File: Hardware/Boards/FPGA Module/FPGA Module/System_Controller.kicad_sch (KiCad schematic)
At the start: 0 parts

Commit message: FPGA Board schematic work
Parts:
- added C1, C10, C11, C5, C6, C7, C8, C9: 100nF, Capacitor_SMD:C_0201_0603Metric, symbol Device:C_Small
- added C12, C4: 1uF, Capacitor_SMD:C_0201_0603Metric, symbol Device:C_Small
- added C2, C3: 18pF, Capacitor_SMD:C_0201_0603Metric, symbol Device:C_Small
- added D1: MCU Heartbeat, LED_SMD:LED_0603_1608Metric, symbol Device:LED
- added R1: 10K, Resistor_SMD:R_0201_0603Metric, symbol Device:R_US
- added R2: 1K, Resistor_SMD:R_0201_0603Metric, symbol Device:R_US
- added SW1: RST, Button_Switch_SMD:SW_Push_SPST_NO_Alps_SKRK, symbol Switch:SW_SPST
- added TP1, TP2: TestPoint, TestPoint:TestPoint_Pad_D1.0mm, symbol Connector:TestPoint
- added U11: TPS74801AWDRC, Package_SON:VSON-10-1EP_3x3mm_P0.5mm_EP1.65x2.4mm_ThermalVias, symbol Regulator_Linear:TPS74801AWDRC
- added U5: W25Q16JVUXIQ TR, IO_Module:USON-8_UX_2x3x0p6_WIN, symbol Memory_Flash:W25Q16JVUXIQ_TR
- added U6: RP2040, Package_DFN_QFN:QFN-56-1EP_7x7mm_P0.4mm_EP3.2x3.2mm, symbol MCU_RaspberryPi:RP2040
- added Y1: 12Mhz, Oscillator:Oscillator_SMD_Abracon_ASE-4Pin_3.2x2.5mm, symbol Device:Crystal_GND24_Small
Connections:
- new net: TP2.1, U6.25 (SWD)
- new net: TP1.1, U6.24 (SWCLK)
- new net: D1.2 (A), R2.2
- new net: R1.2, SW1.2 (B)
- new net: U11.1 (IN), U11.2 (IN)
- new net: U11.10 (OUT), U11.9 (OUT)
- new net: U11.11 (GND), U11.6 (GND)
- new net +3V3: C1.1, U5.8 (VCC)
- new net +3V3_MCU: C10.1, C11.1, C12.1, C7.1, C8.1, C9.1, U6.1 (IOVDD), U6.10 (IOVDD), U6.22 (IOVDD), U6.33 (IOVDD), U6.42 (IOVDD), U6.43 (ADC_AVDD), U6.44 (VREG_IN), U6.48 (USB_VDD), U6.49 (IOVDD)
- new net GND: C1.2, C10.2, C11.2, C12.2, C2.2, C3.2, C4.2, C5.2, C6.2, C7.2, C8.2, C9.2, D1.1 (K), SW1.1 (A), U5.4 (GND), U5.9 (EPAD), U6.19 (TESTEN), U6.57 (GND), Y1.2, Y1.4
- new net I2C0_SCL: U6.7 (GPIO5)
- new net I2C0_SDA: U6.6 (GPIO4)
- new net I2C1_SCL: U6.9 (GPIO7)
- new net I2C1_SDA: U6.8 (GPIO6)
- new net MCU_HB_LED: R2.1, U6.37 (GPIO25)
- new net MCU_XI: C2.1, U6.20 (XIN), Y1.1
- new net MCU_XO: C3.1, U6.21 (XOUT), Y1.3
- new net QSPI_CLK: U5.6 (CLK), U6.52 (QSPI_SCLK)
- new net QSPI_CS: R1.1, U5.1 (/CS), U6.56 (QSPI_SS)
- new net QSPI_D0: U5.5 (DI(IO0)), U6.53 (QSPI_SD0)
- new net QSPI_D1: U5.2 (DO(IO1)), U6.55 (QSPI_SD1)
- new net QSPI_D2: U5.3 (/WP(IO2)), U6.54 (QSPI_SD2)
- new net QSPI_D3: U5.7 (/HLD/RST(IO3)), U6.51 (QSPI_SD3)
- new net USB_SYSMON_D_N: U6.46 (USB_DM)
- new net USB_SYSMON_D_P: U6.47 (USB_DP)
- new net VMCU_1V1: C4.1, C5.1, C6.1, U6.23 (DVDD), U6.45 (VREG_VOUT), U6.50 (DVDD)
- no-connect marks 0 -> 1
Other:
- note added: "System Controller MCU"

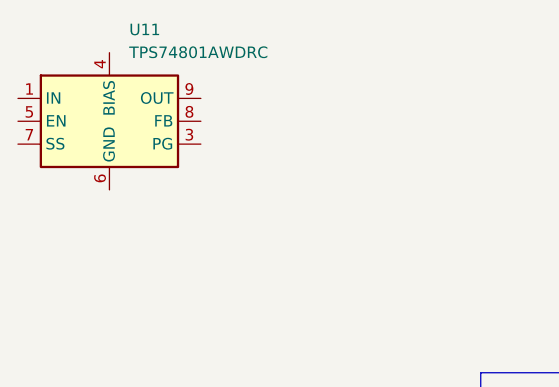
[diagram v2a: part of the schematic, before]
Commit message: FPGA Module Power Schematic Changes
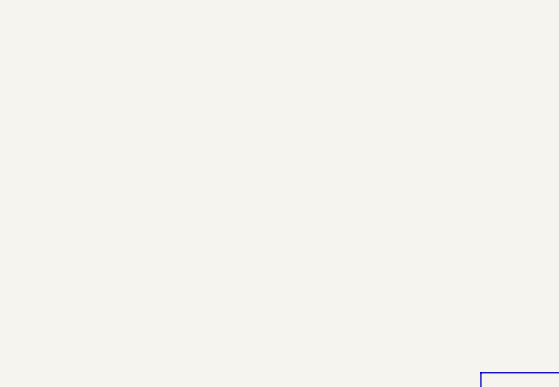
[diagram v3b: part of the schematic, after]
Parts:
- removed U11: TPS74801AWDRC, Package_SON:VSON-10-1EP_3x3mm_P0.5mm_EP1.65x2.4mm_ThermalVias, symbol Regulator_Linear:TPS74801AWDRC
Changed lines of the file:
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@@
-	)
-	(symbol
-		(lib_id "Regulator_Linear:TPS74801AWDRC")
-		(at 59.69 40.64 0)
-		(unit 1)
-		(exclude_from_sim no)
-		(in_bom yes)
-		(on_board yes)
-		(dnp no)
-		(fields_autoplaced yes)
-		(property "Reference" "U11"
-			(at 61.8841 30.48 0)
-			(effects
-				(font
-					(size 1.27 1.27)
-				)
-				(justify left)
-			)
-		)
-		(property "Value" "TPS74801AWDRC"
-			(at 61.8841 33.02 0)
-			(effects
-				(font
-					(size 1.27 1.27)
-				)
-				(justify left)
-			)
-		)
-		(property "Footprint" "Package_SON:VSON-10-1EP_3x3mm_P0.5mm_EP1.65x2.4mm_ThermalVias"
-			(at 59.69 30.48 0)
-			(effects
-				(font
-					(size 1.27 1.27)
-				)
-				(hide yes)
-			)
-		)
-		(property "Datasheet" "https://www.ti.com/lit/ds/symlink/tps748a.pdf"
-			(at 59.69 27.94 0)
-			(effects
-				(font
-					(size 1.27 1.27)
-				)
-				(hide yes)
-			)
-		)
-		(property "Description" "Texas Instruments 1.5A, Low-Dropout Linear Regulator With Programmable Soft-Start, 0.8-6.0Vin, 2.7-6.0Vbias, 0.8-3.6Vout"
-			(at 59.69 40.64 0)
-			(effects
-				(font
-					(size 1.27 1.27)
-				)
-				(hide yes)
-			)
-		)
-		(pin "2"
-		)
-		(pin "5"
-		)
-		(pin "7"
-		)
-		(pin "9"
-		)
-		(pin "1"
-		)
-		(pin "4"
-		)
-		(pin "3"
-		)
-		(pin "10"
-		)
-		(pin "6"
-		)
-		(pin "8"
-		)
-		(pin "11"
-		)
-		(instances
-			(project ""
-				(path "/199f10e2-d4b4-4a27-9e84-7b1ce2ae6bf0/0c296310-f788-47f0-8a3f-43c3444563e8/dc5b5b57-015e-40a7-96b0-c580a953f4f8"
-					(reference "U11")
-					(unit 1)
-				)
-			)
-		)
 	)
 	(symbol

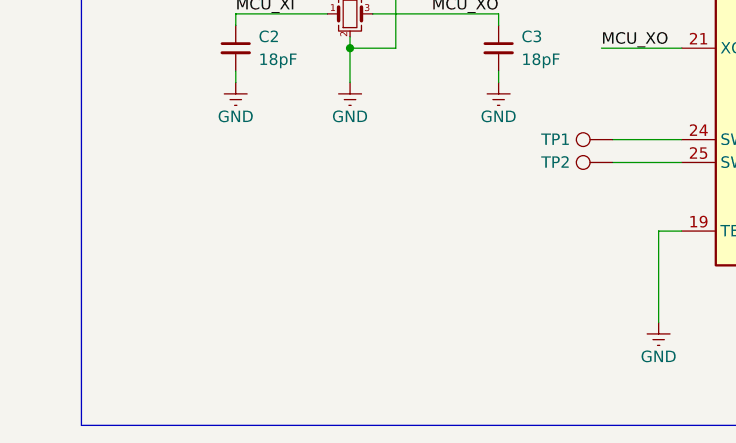
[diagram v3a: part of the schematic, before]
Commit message: Using new DP to HDMI IC
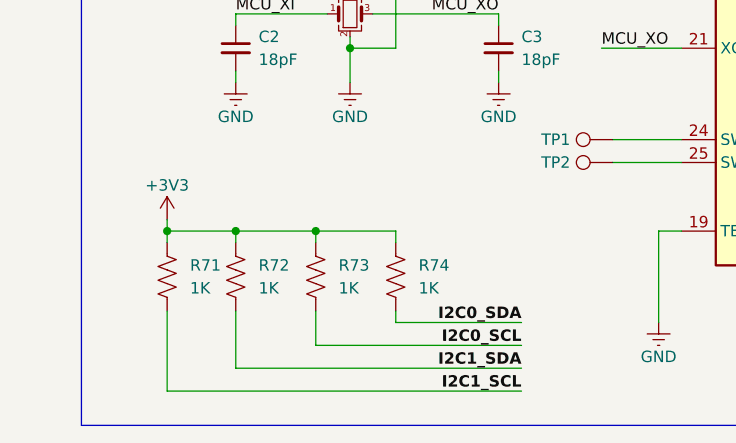
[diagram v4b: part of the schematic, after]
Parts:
- added R71, R72, R73, R74: 1K, Resistor_SMD:R_0402_1005Metric, symbol Device:R_US
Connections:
- net +3V3: now also R71.2, R72.2, R73.2, R74.2
- net I2C0_SCL: now also R73.1
- net I2C0_SDA: now also R74.1
- net I2C1_SCL: now also R71.1
- net I2C1_SDA: now also R72.1

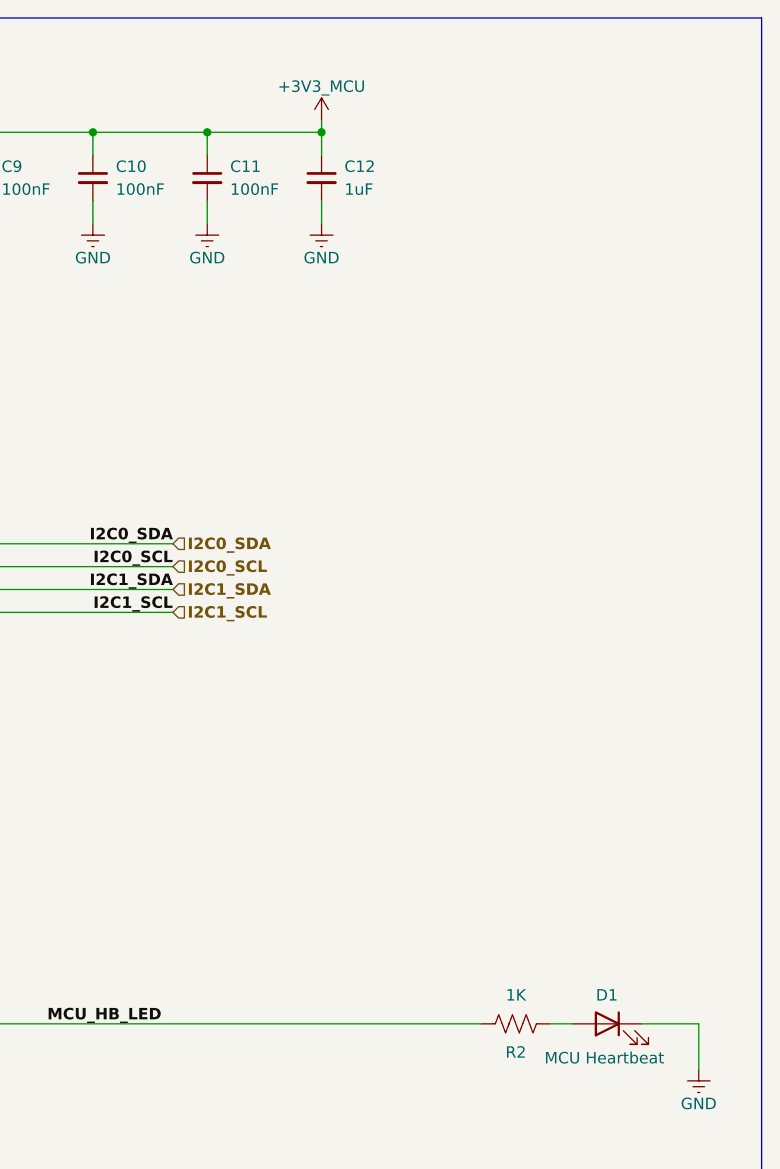
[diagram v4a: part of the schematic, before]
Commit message: updated fpga module schematics
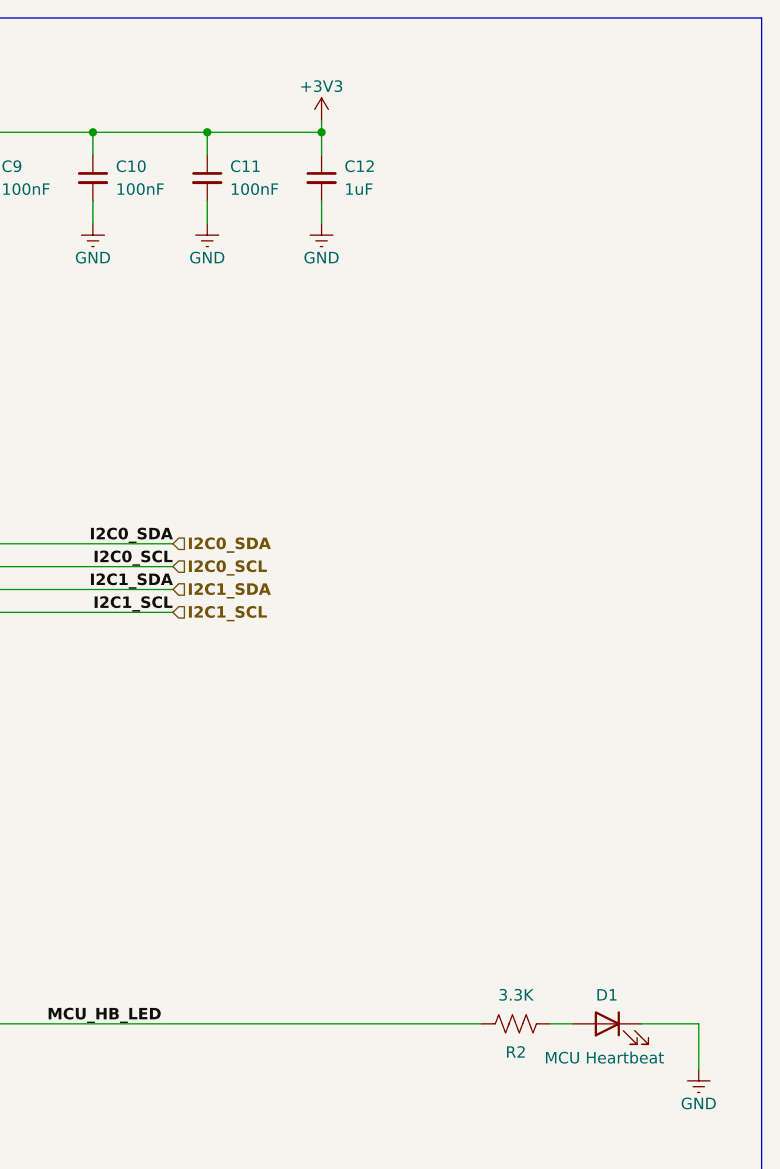
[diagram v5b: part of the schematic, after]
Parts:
- R2: value 1K -> 3.3K
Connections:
- net +3V3_MCU is gone; now on net +3V3: C10.1, C11.1, C12.1, C7.1, C8.1, C9.1, U6.1 (IOVDD), U6.10 (IOVDD), U6.22 (IOVDD), U6.33 (IOVDD), U6.42 (IOVDD), U6.43 (ADC_AVDD), U6.44 (VREG_IN), U6.48 (USB_VDD), U6.49 (IOVDD)
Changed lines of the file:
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@@
+	)
+	(symbol
+		(lib_id "power:+3V3")
+		(at 260.35 80.01 0)
+		(unit 1)
+		(exclude_from_sim no)
+		(in_bom yes)
+		(on_board yes)
+		(dnp no)
+		(property "Reference" "#PWR017"
+			(at 260.35 83.82 0)
+			(effects
+				(font
+					(size 1.27 1.27)
+				)
+				(hide yes)
+			)
+		)
+		(property "Value" "+3V3"
+			(at 260.35 76.2 0)
+			(effects
+				(font
+					(size 1.27 1.27)
+				)
+			)
+		)
+		(property "Footprint" ""
+			(at 260.35 80.01 0)
+			(effects
+				(font
+					(size 1.27 1.27)
+				)
+				(hide yes)
+			)
+		)
+		(property "Datasheet" ""
+			(at 260.35 80.01 0)
+			(effects
+				(font
+					(size 1.27 1.27)
+				)
+				(hide yes)
+			)
+		)
+		(property "Description" "Power symbol creates a global label with name \"+3V3\""
+			(at 260.35 80.01 0)
+			(effects
+				(font
+					(size 1.27 1.27)
+				)
+				(hide yes)
+			)
+		)
+		(pin "1"
+		)
+		(instances
+			(project "FPGA Module"
+				(path "/199f10e2-d4b4-4a27-9e84-7b1ce2ae6bf0/0c296310-f788-47f0-8a3f-43c3444563e8/dc5b5b57-015e-40a7-96b0-c580a953f4f8"
+					(reference "#PWR017")
+					(unit 1)
+				)
+			)
+		)
 	)
 	(symbol
@@
 			)
 		)
-		(property "Value" "1K"
+		(property "Value" "3.3K"
 			(at 281.94 177.165 90)
 			(effects
@@
 					(unit 1)
 				)
-			)
-		)
-	)
-	(symbol
-		(lib_id "power:+3V3")
-		(at 260.35 80.01 0)
-		(unit 1)
-		(exclude_from_sim no)
-		(in_bom yes)
-		(on_board yes)
-		(dnp no)
-		(property "Reference" "#PWR017"
-			(at 260.35 83.82 0)
-			(effects
-				(font
-					(size 1.27 1.27)
-				)
-				(hide yes)
-			)
-		)
-		(property "Value" "+3V3_MCU"
-			(at 260.35 76.2 0)
-			(effects
-				(font
-					(size 1.27 1.27)
-				)
-			)
-		)
-		(property "Footprint" ""
-			(at 260.35 80.01 0)
-			(effects
-				(font
-					(size 1.27 1.27)
-				)
-				(hide yes)
-			)
-		)
-		(property "Datasheet" ""
-			(at 260.35 80.01 0)
-			(effects
-				(font
-					(size 1.27 1.27)
-				)
-				(hide yes)
-			)
-		)
-		(property "Description" "Power symbol creates a global label with name \"+3V3\""
-			(at 260.35 80.01 0)
-			(effects
-				(font
-					(size 1.27 1.27)
-				)
-				(hide yes)
-			)
-		)
-		(pin "1"
-		)
-		(instances
-			(project "FPGA Module"
-				(path "/199f10e2-d4b4-4a27-9e84-7b1ce2ae6bf0/0c296310-f788-47f0-8a3f-43c3444563e8/dc5b5b57-015e-40a7-96b0-c580a953f4f8"
-					(reference "#PWR017")
-					(unit 1)
-				)

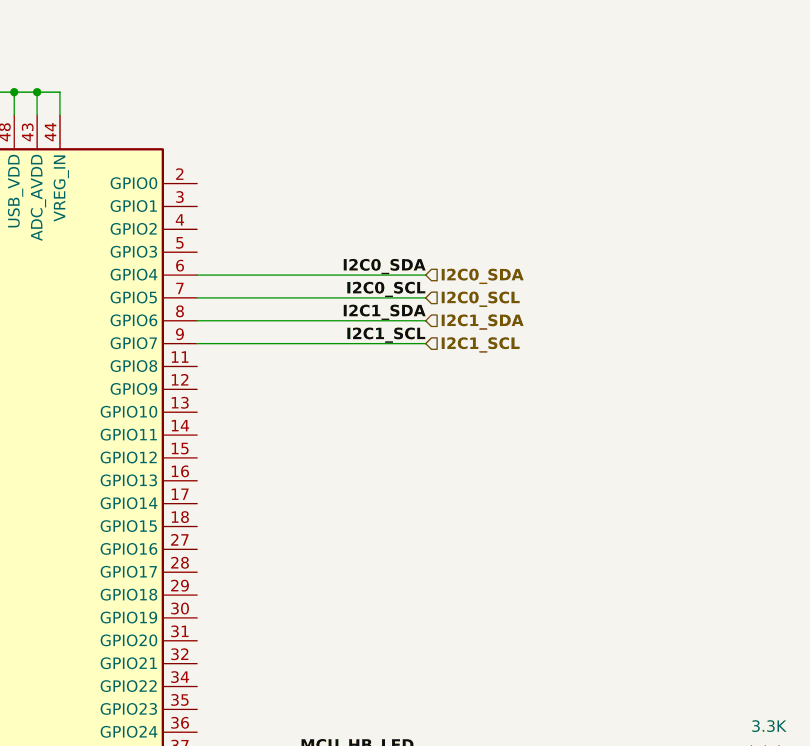
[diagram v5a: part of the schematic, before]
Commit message: Added Top sheet connections for FPGA module
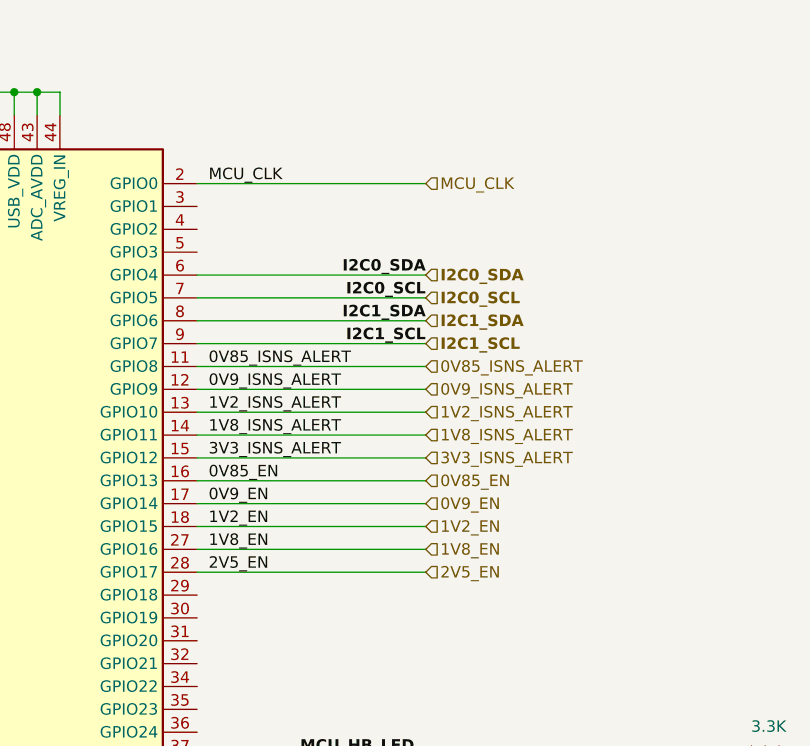
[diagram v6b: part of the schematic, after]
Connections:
- net 0V85_ISNS_ALERT: now reaches U6.11 (GPIO8)
- net 0V9_ISNS_ALERT: now reaches U6.12 (GPIO9)
- net 1V2_ISNS_ALERT: now reaches U6.13 (GPIO10)
- net 1V8_ISNS_ALERT: now reaches U6.14 (GPIO11)
- net 3V3_ISNS_ALERT: now reaches U6.15 (GPIO12)
- net 0V85_EN: now reaches U6.16 (GPIO13)
- net 0V9_EN: now reaches U6.17 (GPIO14)
- net 1V2_EN: now reaches U6.18 (GPIO15)
- net MCU_CLK: now reaches U6.2 (GPIO0)
- net 1V8_EN: now reaches U6.27 (GPIO16)
- net 2V5_EN: now reaches U6.28 (GPIO17)

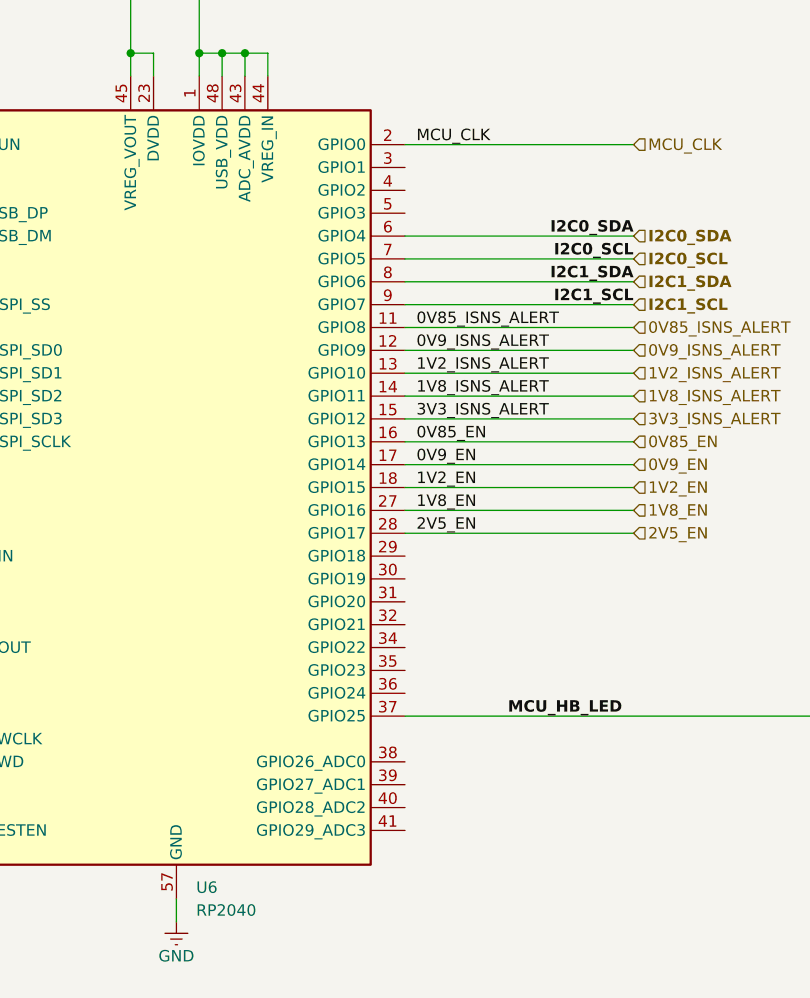
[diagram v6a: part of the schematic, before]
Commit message: Added NC to unused pins
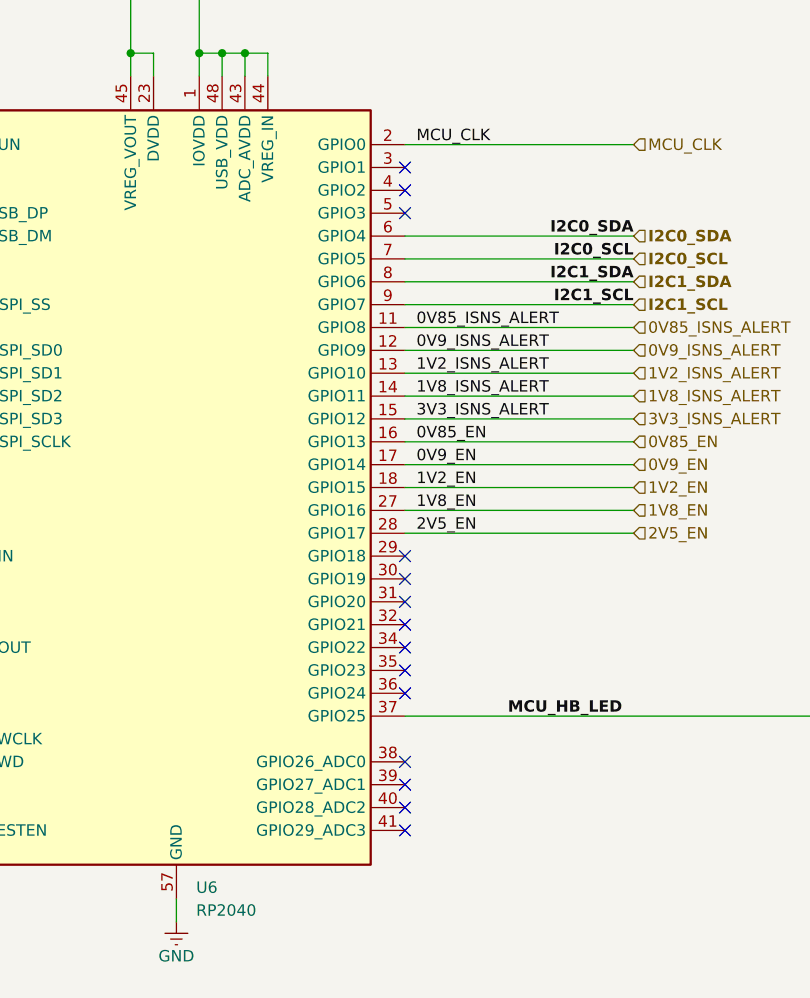
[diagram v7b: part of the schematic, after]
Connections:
- no-connect marks 1 -> 15
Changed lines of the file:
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@@
+	)
+	(no_connect
+		(at 218.44 121.92)
+	)
+	(no_connect
+		(at 218.44 193.04)
+	)
+	(no_connect
+		(at 218.44 172.72)
+	)
+	(no_connect
+		(at 218.44 185.42)
+	)
+	(no_connect
+		(at 218.44 187.96)
+	)
+	(no_connect
+		(at 218.44 175.26)
+	)
+	(no_connect
+		(at 218.44 177.8)
+	)
+	(no_connect
+		(at 218.44 162.56)
+	)
+	(no_connect
+		(at 218.44 170.18)
+	)
+	(no_connect
+		(at 218.44 190.5)
+	)
+	(no_connect
+		(at 218.44 119.38)
+	)
+	(no_connect
+		(at 218.44 124.46)
+	)
+	(no_connect
+		(at 218.44 165.1)
 	)
 	(no_connect
 		(at 167.64 116.84)
 	)
+	(no_connect
+		(at 218.44 167.64)
+	)
 	(wire
